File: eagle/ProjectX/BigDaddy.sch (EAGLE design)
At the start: 4 parts, among them U1 TC4427AEOA

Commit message: Working on the big board
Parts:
- added C1, C3, C5, C6: (no value), resistor:C-EUC0805
- added SP10, SP11, SP12, SP5, SP6, SP9: MA40S4S, Parts:MA40S4S
- added U3, U5, U6: TC4427AEOA, Parts:TC4427AEOA
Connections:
- new net N$10: SP6.2, U3.*OUT_B
- new net N$13: SP11.2, U6.*OUT_A
- new net N$14: SP12.2, U6.*OUT_B
- new net N$7: SP9.2, U5.*OUT_A
- new net N$8: SP10.2, U5.*OUT_B
- new net N$9: SP5.2, U3.*OUT_A
- new net VDD: C1.2, C3.2, C5.2, C6.2, U1.VDD, U3.VDD, U5.VDD, U6.VDD
- net +5V: no longer U1.VDD
- net GND: now also C1.1, C3.1, C5.1, C6.1, SP10.1, SP11.1, SP12.1, SP5.1, SP6.1, SP9.1, U3.GND, U5.GND, U6.GND
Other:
- moved on the sheet: SP1, SP2, U1

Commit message: Layout of transducers complete, need to add connectors, power, and then route everything
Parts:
- removed C1, C6: (no value), resistor:C-EUC0805
- removed SP1, SP11, SP12, SP2: MA40S4S, Parts:MA40S4S
- removed U1, U6: TC4427AEOA, Parts:TC4427AEOA
- added C10, C11, C12, C13, C19, C20, C21, C22, C23, C24, C25, C26, C27, C28, C29, C30, C31, C32, C34, C35, C36, C37, C38, C39, C4, C40, C41, C42, C43, C44, C45, C55, C56, C57, C58, C59, C60, C61, C62, C63, C7, C9: (no value), resistor:C-EUC0805
- added SP109, SP110, SP111, SP112, SP113, SP114, SP115, SP116, SP117, SP118, SP119, SP120, SP121, SP122, SP123, SP124, SP125, SP126, SP13, SP14, SP17, SP18, SP19, SP20, SP21, SP22, SP23, SP24, SP25, SP26, SP37, SP38, SP39, SP40, SP41, SP42, SP43, SP44, SP45, SP46, SP47, SP48, SP49, SP50, SP51, SP52, SP53, SP54, SP55, SP56, SP57, SP58, SP59, SP60, SP61, SP62, SP63, SP64, SP67, SP68, SP69, SP7, SP70, SP71, SP72, SP73, SP74, SP75, SP76, SP77, SP78, SP79, SP8, SP80, SP81, SP82, SP83, SP84, SP85, SP86, SP87, SP88, SP89, SP90: MA40S4S, Parts:MA40S4S
- added U10, U11, U12, U13, U19, U20, U21, U22, U23, U24, U25, U26, U27, U28, U29, U30, U31, U32, U34, U35, U36, U37, U38, U39, U4, U40, U41, U42, U43, U44, U45, U55, U56, U57, U58, U59, U60, U61, U62, U63, U7, U9: TC4427AEOA, Parts:TC4427AEOA
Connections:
- removed net N$1: SP1.2, U1.*OUT_A
- removed net N$13: SP11.2, U6.*OUT_A
- removed net N$14: SP12.2, U6.*OUT_B
- removed net N$2: SP2.2, U1.*OUT_B
- new net N$111: SP109.2, U55.*OUT_A
- new net N$112: SP110.2, U55.*OUT_B
- new net N$113: SP111.2, U56.*OUT_A
- new net N$114: SP112.2, U56.*OUT_B
- new net N$115: SP113.2, U57.*OUT_A
- new net N$116: SP114.2, U57.*OUT_B
- new net N$117: SP115.2, U58.*OUT_A
- new net N$118: SP116.2, U58.*OUT_B
- new net N$119: SP117.2, U59.*OUT_A
- new net N$120: SP118.2, U59.*OUT_B
- new net N$121: SP119.2, U60.*OUT_A
- new net N$122: SP120.2, U60.*OUT_B
- new net N$123: SP121.2, U61.*OUT_A
- new net N$124: SP122.2, U61.*OUT_B
- new net N$125: SP123.2, U62.*OUT_A
- new net N$126: SP124.2, U62.*OUT_B
- new net N$127: SP125.2, U63.*OUT_A
- new net N$128: SP126.2, U63.*OUT_B
- new net N$15: SP13.2, U7.*OUT_A
- new net N$16: SP14.2, U7.*OUT_B
- new net N$19: SP17.2, U9.*OUT_A
- new net N$20: SP18.2, U9.*OUT_B
- new net N$21: SP19.2, U10.*OUT_A
- new net N$22: SP20.2, U10.*OUT_B
- new net N$23: SP21.2, U11.*OUT_A
- new net N$24: SP22.2, U11.*OUT_B
- new net N$25: SP23.2, U12.*OUT_A
- new net N$26: SP24.2, U12.*OUT_B
- new net N$27: SP25.2, U13.*OUT_A
- new net N$28: SP26.2, U13.*OUT_B
- new net N$39: SP37.2, U19.*OUT_A
- new net N$40: SP38.2, U19.*OUT_B
- new net N$41: SP39.2, U20.*OUT_A
- new net N$42: SP40.2, U20.*OUT_B
- new net N$43: SP41.2, U21.*OUT_A
- new net N$44: SP42.2, U21.*OUT_B
- new net N$45: SP43.2, U22.*OUT_A
- new net N$46: SP44.2, U22.*OUT_B
- new net N$47: SP45.2, U23.*OUT_A
- new net N$48: SP46.2, U23.*OUT_B
- new net N$49: SP47.2, U24.*OUT_A
- new net N$50: SP48.2, U24.*OUT_B
- new net N$51: SP49.2, U25.*OUT_A
- new net N$52: SP50.2, U25.*OUT_B
- new net N$53: SP51.2, U26.*OUT_A
- new net N$54: SP52.2, U26.*OUT_B
- new net N$55: SP53.2, U27.*OUT_A
- new net N$56: SP54.2, U27.*OUT_B
- new net N$57: SP55.2, U28.*OUT_A
- new net N$58: SP56.2, U28.*OUT_B
- new net N$59: SP57.2, U29.*OUT_A
- new net N$60: SP58.2, U29.*OUT_B
- new net N$61: SP59.2, U30.*OUT_A
- new net N$62: SP60.2, U30.*OUT_B
- new net N$63: SP61.2, U31.*OUT_A
- new net N$64: SP62.2, U31.*OUT_B
- new net N$65: SP63.2, U32.*OUT_A
- new net N$66: SP64.2, U32.*OUT_B
- new net N$69: SP67.2, U34.*OUT_A
- new net N$7: SP7.2, U4.*OUT_A
- new net N$70: SP68.2, U34.*OUT_B
- new net N$71: SP69.2, U35.*OUT_A
- new net N$72: SP70.2, U35.*OUT_B
- new net N$73: SP71.2, U36.*OUT_A
- new net N$74: SP72.2, U36.*OUT_B
- new net N$75: SP73.2, U37.*OUT_A
- new net N$76: SP74.2, U37.*OUT_B
- new net N$77: SP75.2, U38.*OUT_A
- new net N$78: SP76.2, U38.*OUT_B
- new net N$79: SP77.2, U39.*OUT_A
- new net N$8: SP8.2, U4.*OUT_B
- new net N$80: SP78.2, U39.*OUT_B
- new net N$81: SP79.2, U40.*OUT_A
- new net N$82: SP80.2, U40.*OUT_B
- new net N$83: SP81.2, U41.*OUT_A
- new net N$84: SP82.2, U41.*OUT_B
- new net N$85: SP83.2, U42.*OUT_A
- new net N$86: SP84.2, U42.*OUT_B
- new net N$87: SP85.2, U43.*OUT_A
- new net N$88: SP86.2, U43.*OUT_B
- new net N$89: SP87.2, U44.*OUT_A
- new net N$90: SP88.2, U44.*OUT_B
- new net N$91: SP89.2, U45.*OUT_A
- new net N$92: SP90.2, U45.*OUT_B
- net GND: now also C10.1, C11.1, C12.1, C13.1, C19.1, C20.1, C21.1, C22.1, C23.1, C24.1, C25.1, C26.1, C27.1, C28.1, C29.1, C30.1, C31.1, C32.1, C34.1, C35.1, C36.1, C37.1, C38.1, C39.1, C4.1, C40.1, C41.1, C42.1, C43.1, C44.1, C45.1, C55.1, C56.1, C57.1, C58.1, C59.1, C60.1, C61.1, C62.1, C63.1, C7.1, C9.1, SP109.1, SP110.1, SP111.1, SP112.1, SP113.1, SP114.1, SP115.1, SP116.1, SP117.1, SP118.1, SP119.1, SP120.1, SP121.1, SP122.1, SP123.1, SP124.1, SP125.1, SP126.1, SP13.1, SP14.1, SP17.1, SP18.1, SP19.1, SP20.1, SP21.1, SP22.1, SP23.1, SP24.1, SP25.1, SP26.1, SP37.1, SP38.1, SP39.1, SP40.1, SP41.1, SP42.1, SP43.1, SP44.1, SP45.1, SP46.1, SP47.1, SP48.1, SP49.1, SP50.1, SP51.1, SP52.1, SP53.1, SP54.1, SP55.1, SP56.1, SP57.1, SP58.1, SP59.1, SP60.1, SP61.1, SP62.1, SP63.1, SP64.1, SP67.1, SP68.1, SP69.1, SP7.1, SP70.1, SP71.1, SP72.1, SP73.1, SP74.1, SP75.1, SP76.1, SP77.1, SP78.1, SP79.1, SP8.1, SP80.1, SP81.1, SP82.1, SP83.1, SP84.1, SP85.1, SP86.1, SP87.1, SP88.1, SP89.1, SP90.1, U10.GND, U11.GND, U12.GND, U13.GND, U19.GND, U20.GND, U21.GND, U22.GND, U23.GND, U24.GND, U25.GND, U26.GND, U27.GND, U28.GND, U29.GND, U30.GND, U31.GND, U32.GND, U34.GND, U35.GND, U36.GND, U37.GND, U38.GND, U39.GND, U4.GND, U40.GND, U41.GND, U42.GND, U43.GND, U44.GND, U45.GND, U55.GND, U56.GND, U57.GND, U58.GND, U59.GND, U60.GND, U61.GND, U62.GND, U63.GND, U7.GND, U9.GND; no longer C1.1, C6.1, SP1.1, SP11.1, SP12.1, SP2.1, U1.GND, U6.GND
- net VDD: now also C10.2, C11.2, C12.2, C13.2, C19.2, C20.2, C21.2, C22.2, C23.2, C24.2, C25.2, C26.2, C27.2, C28.2, C29.2, C30.2, C31.2, C32.2, C34.2, C35.2, C36.2, C37.2, C38.2, C39.2, C4.2, C40.2, C41.2, C42.2, C43.2, C44.2, C45.2, C55.2, C56.2, C57.2, C58.2, C59.2, C60.2, C61.2, C62.2, C63.2, C7.2, C9.2, U10.VDD, U11.VDD, U12.VDD, U13.VDD, U19.VDD, U20.VDD, U21.VDD, U22.VDD, U23.VDD, U24.VDD, U25.VDD, U26.VDD, U27.VDD, U28.VDD, U29.VDD, U30.VDD, U31.VDD, U32.VDD, U34.VDD, U35.VDD, U36.VDD, U37.VDD, U38.VDD, U39.VDD, U4.VDD, U40.VDD, U41.VDD, U42.VDD, U43.VDD, U44.VDD, U45.VDD, U55.VDD, U56.VDD, U57.VDD, U58.VDD, U59.VDD, U60.VDD, U61.VDD, U62.VDD, U63.VDD, U7.VDD, U9.VDD; no longer C1.2, C6.2, U1.VDD, U6.VDD
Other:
- moved on the sheet: C3, C5, SP10, SP5, SP6, SP9, U3, U5

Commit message: Some fixes to placement
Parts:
- added J1: (no value), SparkFun-Connectors:CONN_02LOCK_LONGPADS
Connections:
- net +5V: now also DIP1.5V@1
- net GND: now also J1.2
- net VDD: now also J1.1
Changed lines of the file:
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@@
 <layer number="230" name="230bmp" color="7" fill="1" visible="yes" active="yes"/>
 <layer number="231" name="231bmp" color="7" fill="1" visible="yes" active="yes"/>
+<layer number="232" name="Eagle3D_PG2" color="7" fill="1" visible="yes" active="yes"/>
+<layer number="233" name="Eagle3D_PG3" color="7" fill="1" visible="yes" active="yes"/>
 <layer number="248" name="Housing" color="7" fill="1" visible="yes" active="yes"/>
 <layer number="249" name="Edge" color="7" fill="1" visible="yes" active="yes"/>
@@
 <part name="SUPPLY38" library="SparkFun-PowerSymbols" library_urn="urn:adsk.eagle:library:530" deviceset="VDD" device=""/>
 <part name="C36" library="resistor" library_urn="urn:adsk.eagle:library:348" deviceset="C-EU" device="C0805" package3d_urn="urn:adsk.eagle:package:26137/1"/>
+<part name="J1" library="SparkFun-Connectors" library_urn="urn:adsk.eagle:library:513" deviceset="CONN_02" device="LOCK_LONGPADS" package3d_urn="urn:adsk.eagle:package:38047/1"/>
+<part name="SUPPLY1" library="SparkFun-PowerSymbols" library_urn="urn:adsk.eagle:library:530" deviceset="VDD" device=""/>
+<part name="GND1" library="supply1" library_urn="urn:adsk.eagle:library:371" deviceset="GND" device=""/>
 </parts>
 <sheets>
@@
 <instance part="SUPPLY38" gate="VDD" x="25.4" y="27.94" rot="R270"/>
 <instance part="C36" gate="G$1" x="20.32" y="33.02"/>
+<instance part="J1" gate="G$1" x="246.38" y="-200.66" rot="R90"/>
+<instance part="SUPPLY1" gate="VDD" x="246.38" y="-190.5"/>
+<instance part="GND1" gate="1" x="243.84" y="-187.96" rot="R180"/>
 </instances>
 <busses>
@@
 <junction x="17.78" y="35.56"/>
 </segment>
+<segment>
+<pinref part="J1" gate="G$1" pin="2"/>
+<pinref part="GND1" gate="1" pin="GND"/>
+<wire x1="243.84" y1="-193.04" x2="243.84" y2="-190.5" width="0.1524" layer="91"/>
+</segment>
 </net>
 <net name="+5V" class="0">
@@
 <wire x1="203.2" y1="-63.5" x2="205.74" y2="-63.5" width="0.1524" layer="91"/>
 <pinref part="DIP1" gate="G$1" pin="5V@2"/>
+</segment>
+<segment>
+<pinref part="DIP1" gate="G$1" pin="5V@1"/>
+<pinref part="SUPPLY3" gate="+5V" pin="+5V"/>
+<wire x1="238.76" y1="-63.5" x2="241.3" y2="-63.5" width="0.1524" layer="91"/>
 </segment>
 </net>
@@
 <junction x="20.32" y="27.94"/>
 </segment>
+<segment>
+<pinref part="J1" gate="G$1" pin="1"/>
+<pinref part="SUPPLY1" gate="VDD" pin="VDD"/>
+<wire x1="246.38" y1="-193.04" x2="246.38" y2="-190.5" width="0.1524" layer="91"/>
+</segment>
 </net>

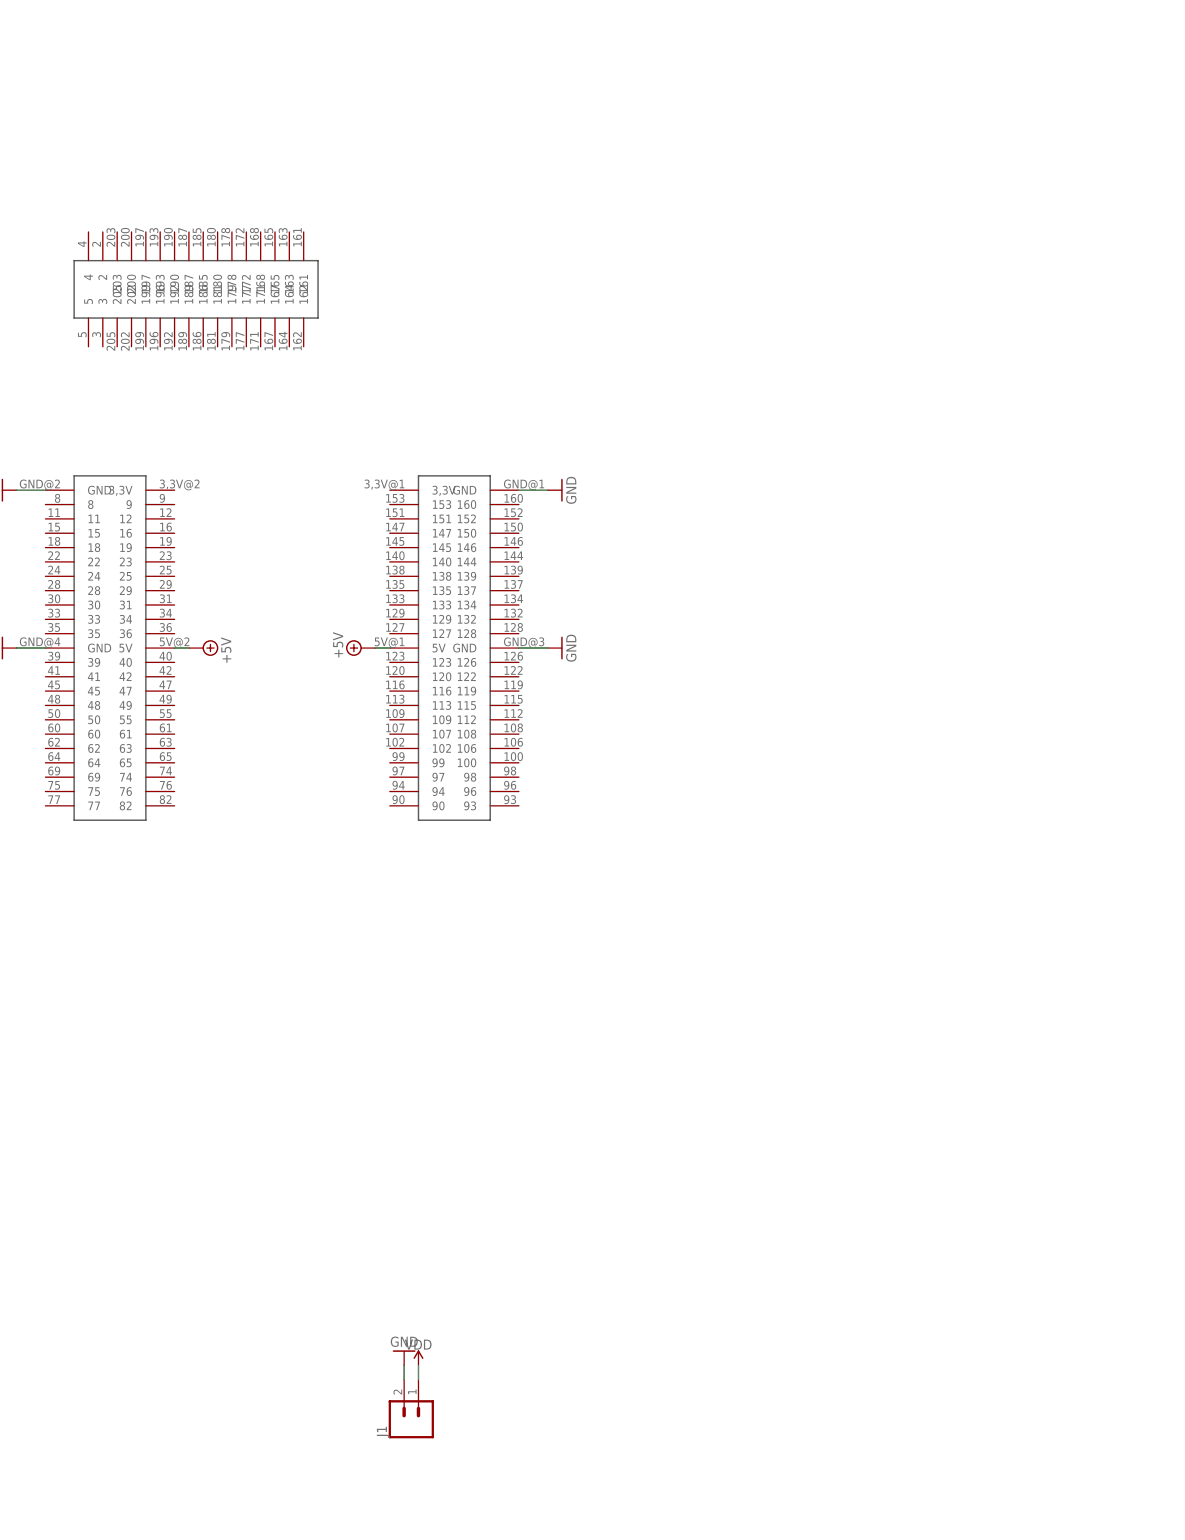
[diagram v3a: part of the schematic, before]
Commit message: Ready to route signal traces
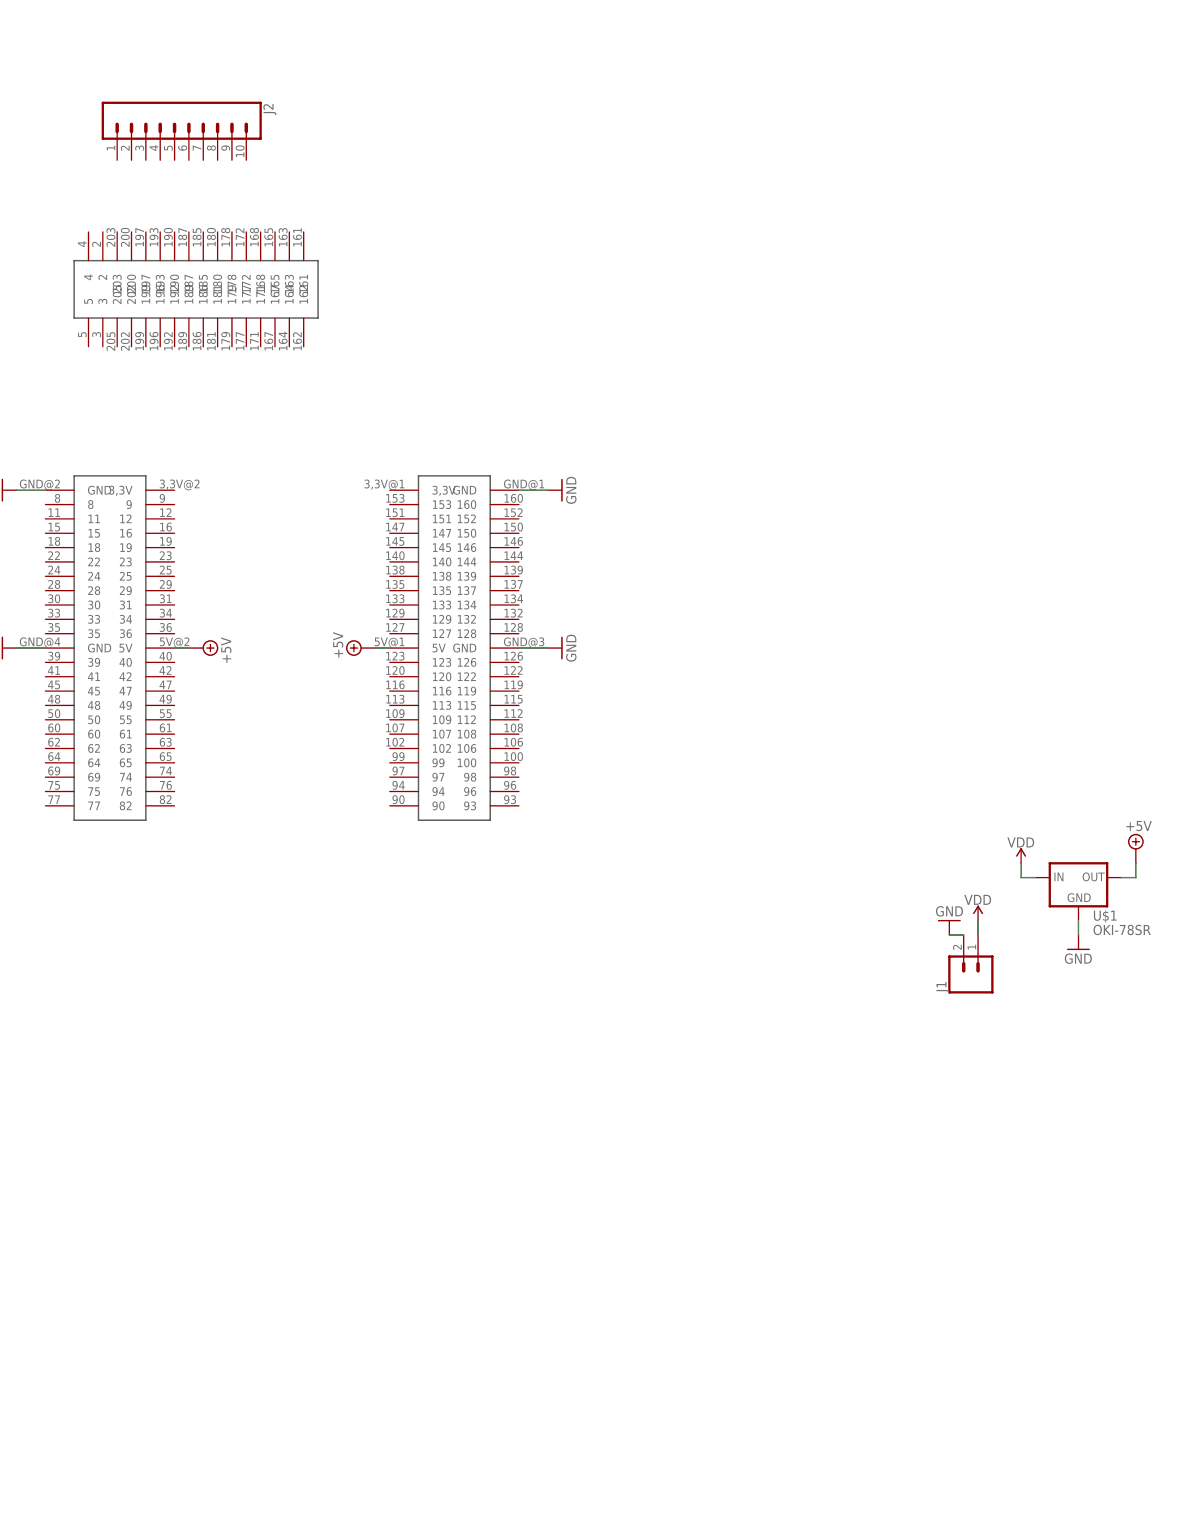
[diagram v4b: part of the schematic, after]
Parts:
- added J2: (no value), SparkFun-Connectors:CONN_10"
- added U$1: OKI-78SR, Parts:OKI-78SR
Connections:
- net +5V: now also U$1.OUT
- net GND: now also U$1.GND
- net VDD: now also U$1.IN
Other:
- moved on the sheet: J1
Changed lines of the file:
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@@
 <part name="SUPPLY1" library="SparkFun-PowerSymbols" library_urn="urn:adsk.eagle:library:530" deviceset="VDD" device=""/>
 <part name="GND1" library="supply1" library_urn="urn:adsk.eagle:library:371" deviceset="GND" device=""/>
+<part name="U$1" library="Parts" deviceset="OKI-78SR" device=""/>
+<part name="GND2" library="supply1" library_urn="urn:adsk.eagle:library:371" deviceset="GND" device=""/>
+<part name="SUPPLY4" library="SparkFun-PowerSymbols" library_urn="urn:adsk.eagle:library:530" deviceset="VDD" device=""/>
+<part name="SUPPLY8" library="supply2" library_urn="urn:adsk.eagle:library:372" deviceset="+5V" device=""/>
+<part name="J2" library="SparkFun-Connectors" library_urn="urn:adsk.eagle:library:513" deviceset="CONN_10" device="&quot;" package3d_urn="urn:adsk.eagle:package:38157/1"/>
 </parts>
 <sheets>
@@
 <instance part="SUPPLY38" gate="VDD" x="25.4" y="27.94" rot="R270"/>
 <instance part="C36" gate="G$1" x="20.32" y="33.02"/>
-<instance part="J1" gate="G$1" x="246.38" y="-200.66" rot="R90"/>
-<instance part="SUPPLY1" gate="VDD" x="246.38" y="-190.5"/>
-<instance part="GND1" gate="1" x="243.84" y="-187.96" rot="R180"/>
+<instance part="J1" gate="G$1" x="345.44" y="-121.92" rot="R90"/>
+<instance part="SUPPLY1" gate="VDD" x="345.44" y="-111.76"/>
+<instance part="GND1" gate="1" x="340.36" y="-111.76" rot="R180"/>
+<instance part="U$1" gate="G$1" x="363.22" y="-104.14"/>
+<instance part="GND2" gate="1" x="363.22" y="-116.84"/>
+<instance part="SUPPLY4" gate="VDD" x="353.06" y="-101.6"/>
+<instance part="SUPPLY8" gate="+5V" x="373.38" y="-99.06"/>
+<instance part="J2" gate="G$1" x="210.82" y="33.02" rot="R270"/>
 </instances>
 <busses>
@@
 <pinref part="J1" gate="G$1" pin="2"/>
 <pinref part="GND1" gate="1" pin="GND"/>
-<wire x1="243.84" y1="-193.04" x2="243.84" y2="-190.5" width="0.1524" layer="91"/>
+<wire x1="342.9" y1="-114.3" x2="340.36" y2="-114.3" width="0.1524" layer="91"/>
+</segment>
+<segment>
+<pinref part="U$1" gate="G$1" pin="GND"/>
+<pinref part="GND2" gate="1" pin="GND"/>
+<wire x1="363.22" y1="-111.76" x2="363.22" y2="-114.3" width="0.1524" layer="91"/>
 </segment>
 </net>
@@
 <pinref part="SUPPLY3" gate="+5V" pin="+5V"/>
 <wire x1="238.76" y1="-63.5" x2="241.3" y2="-63.5" width="0.1524" layer="91"/>
+</segment>
+<segment>
+<pinref part="U$1" gate="G$1" pin="OUT"/>
+<pinref part="SUPPLY8" gate="+5V" pin="+5V"/>
+<wire x1="370.84" y1="-104.14" x2="373.38" y2="-104.14" width="0.1524" layer="91"/>
+<wire x1="373.38" y1="-104.14" x2="373.38" y2="-101.6" width="0.1524" layer="91"/>
 </segment>
 </net>
@@
 <pinref part="J1" gate="G$1" pin="1"/>
 <pinref part="SUPPLY1" gate="VDD" pin="VDD"/>
-<wire x1="246.38" y1="-193.04" x2="246.38" y2="-190.5" width="0.1524" layer="91"/>
+<wire x1="345.44" y1="-114.3" x2="345.44" y2="-111.76" width="0.1524" layer="91"/>
+</segment>
+<segment>
+<pinref part="U$1" gate="G$1" pin="IN"/>
+<pinref part="SUPPLY4" gate="VDD" pin="VDD"/>
+<wire x1="355.6" y1="-104.14" x2="353.06" y2="-104.14" width="0.1524" layer="91"/>
+<wire x1="353.06" y1="-104.14" x2="353.06" y2="-101.6" width="0.1524" layer="91"/>
 </segment>
 </net>
